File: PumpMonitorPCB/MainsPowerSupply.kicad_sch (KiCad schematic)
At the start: 26 parts, among them K1 J115F11CH5VDCS61-5U Relay, Q1 AS2302, U1 ACS770xCB-050B-PFF, U2 AMS1117-3.3

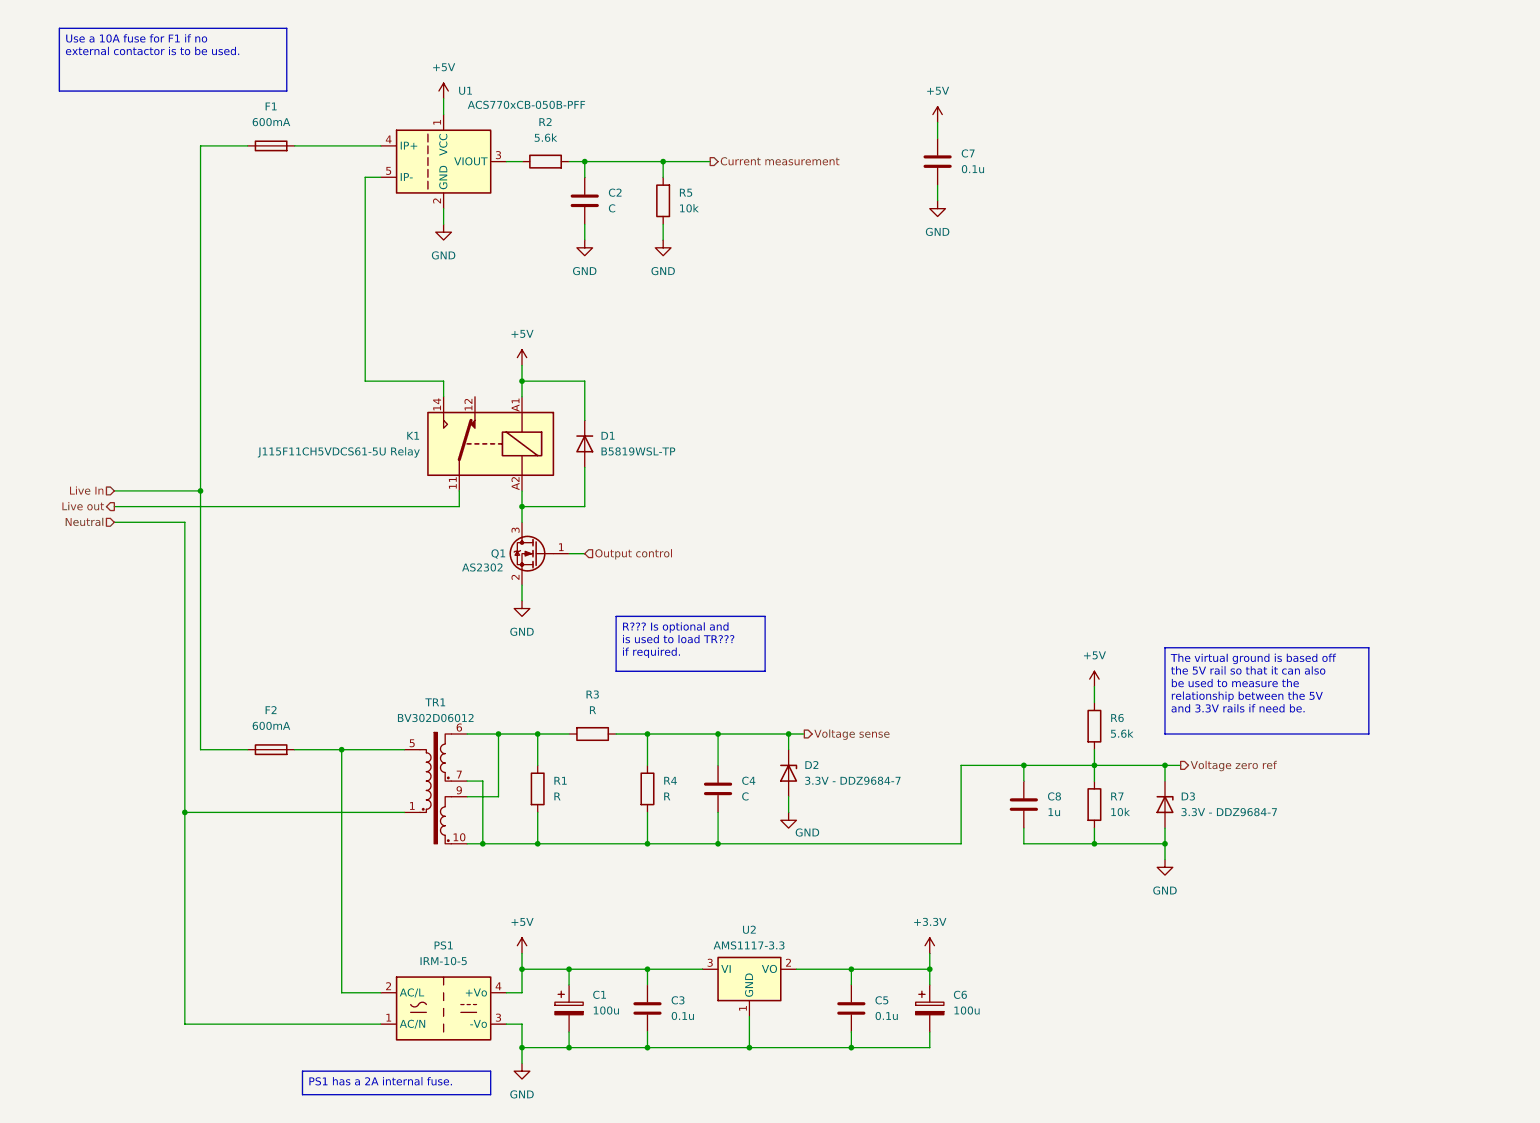
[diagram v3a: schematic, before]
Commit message: Added op amps to voltage and current measurement, more footprint assignments.
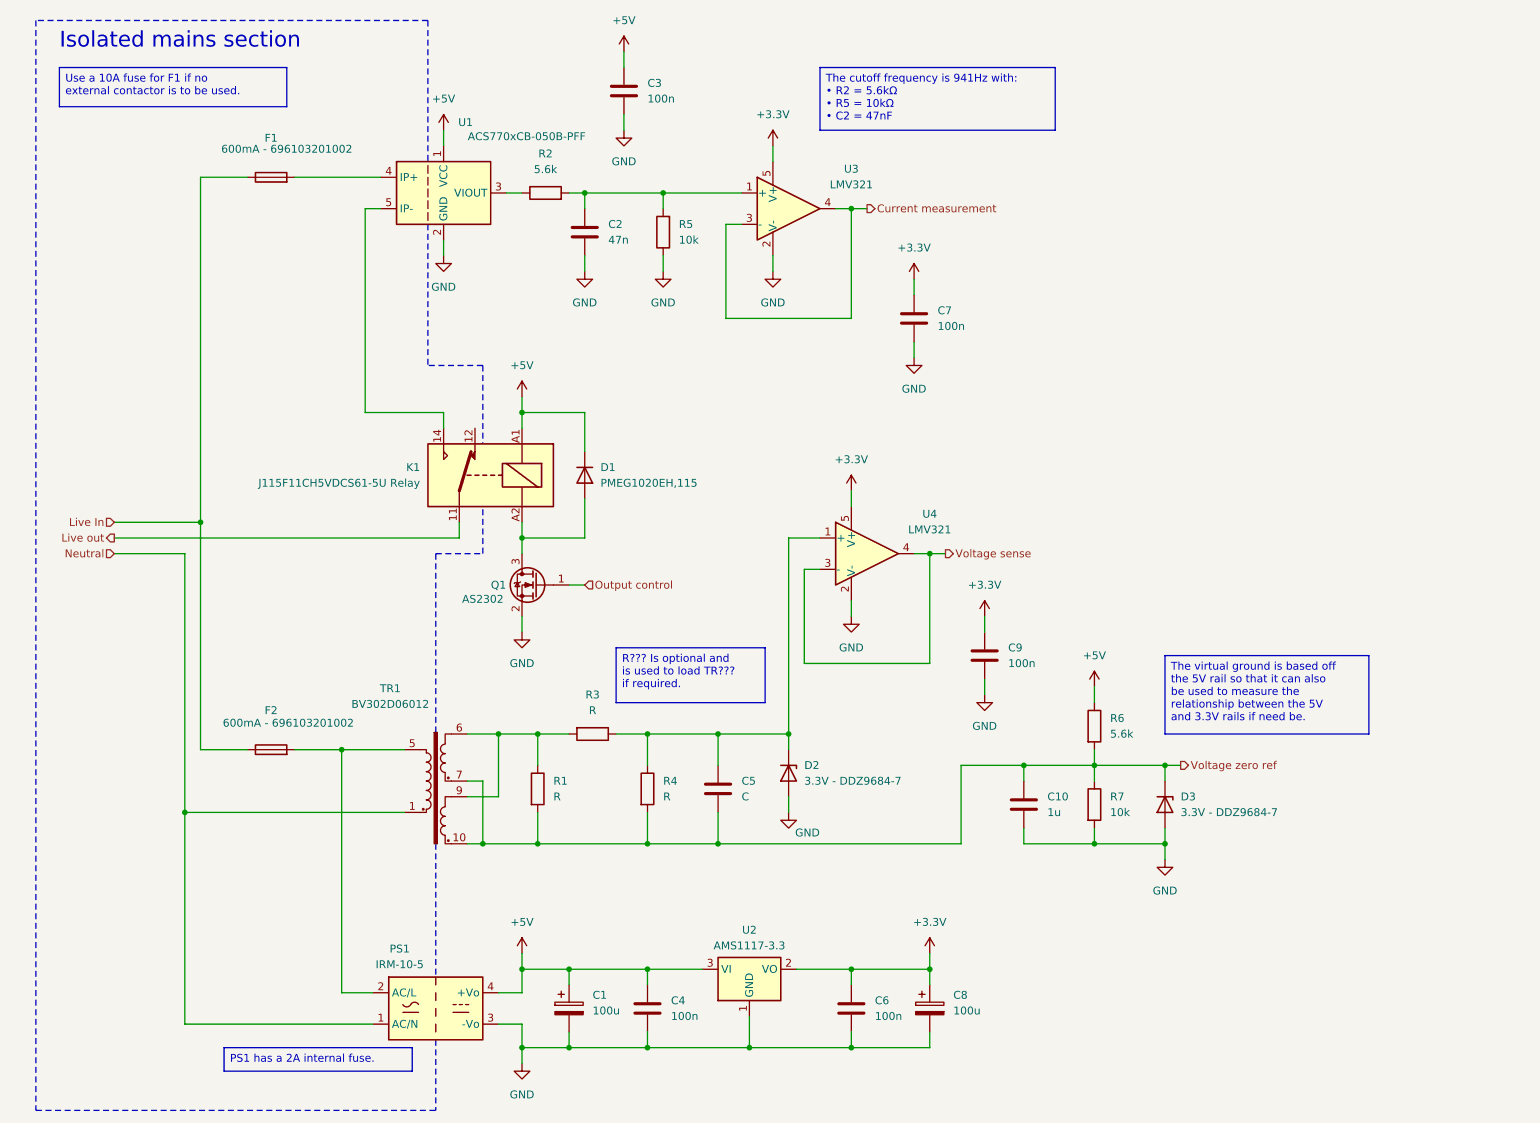
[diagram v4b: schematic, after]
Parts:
- added C7, C9: 100n, Capacitor_SMD:C_0805_2012Metric_Pad1.18x1.45mm_HandSolder, symbol Device:C
- added U3, U4: LMV321, Package_TO_SOT_SMD:SOT-23-5_HandSoldering, symbol Amplifier_Operational:LMV321
- C2: value C -> 47n
- C3: renamed from C7; value 0.1u -> 100n
- C4: renamed from C3; value 0.1u -> 100n
- C6: renamed from C5; value 0.1u -> 100n
- D1: value B5819WSL-TP -> PMEG1020EH,115; footprint Diode_SMD:D_SOD-323F -> Diode_SMD:D_SOD-123F
- F1, F2: value 600mA -> 600mA - 696103201002; footprint (none) -> Fuse:Fuseholder_Cylinder-5x20mm_Stelvio-Kontek_PTF78_Horizontal_Open
- renumbered C8 to C10, C4 to C5, C6 to C8
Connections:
- net +3.3V: now also C7.1, C9.1, U3.5 (V+), U4.5 (V+)
- net Current measurement: now also U3.3 (-), U3.4; no longer C2.1, R2.2, R5.2
- net GND: now also C7.2, C9.2, U3.2 (V-), U4.2 (V-)
- net Voltage sense: now also U4.3 (-), U4.4; no longer C5.1, D2.1 (K), R3.1, R4.1
- new net: C5.1, D2.1 (K), R3.1, R4.1, U4.1 (+)
- new net: C2.1, R2.2, R5.2, U3.1 (+)
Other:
- note added: "Isolated mains section"
- moved on the sheet: C2, C3, D1, F1, K1, PS1, Q1, R2, R5, U1

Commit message: Swapped current measurement to neutral (wiring diagram needs updating).
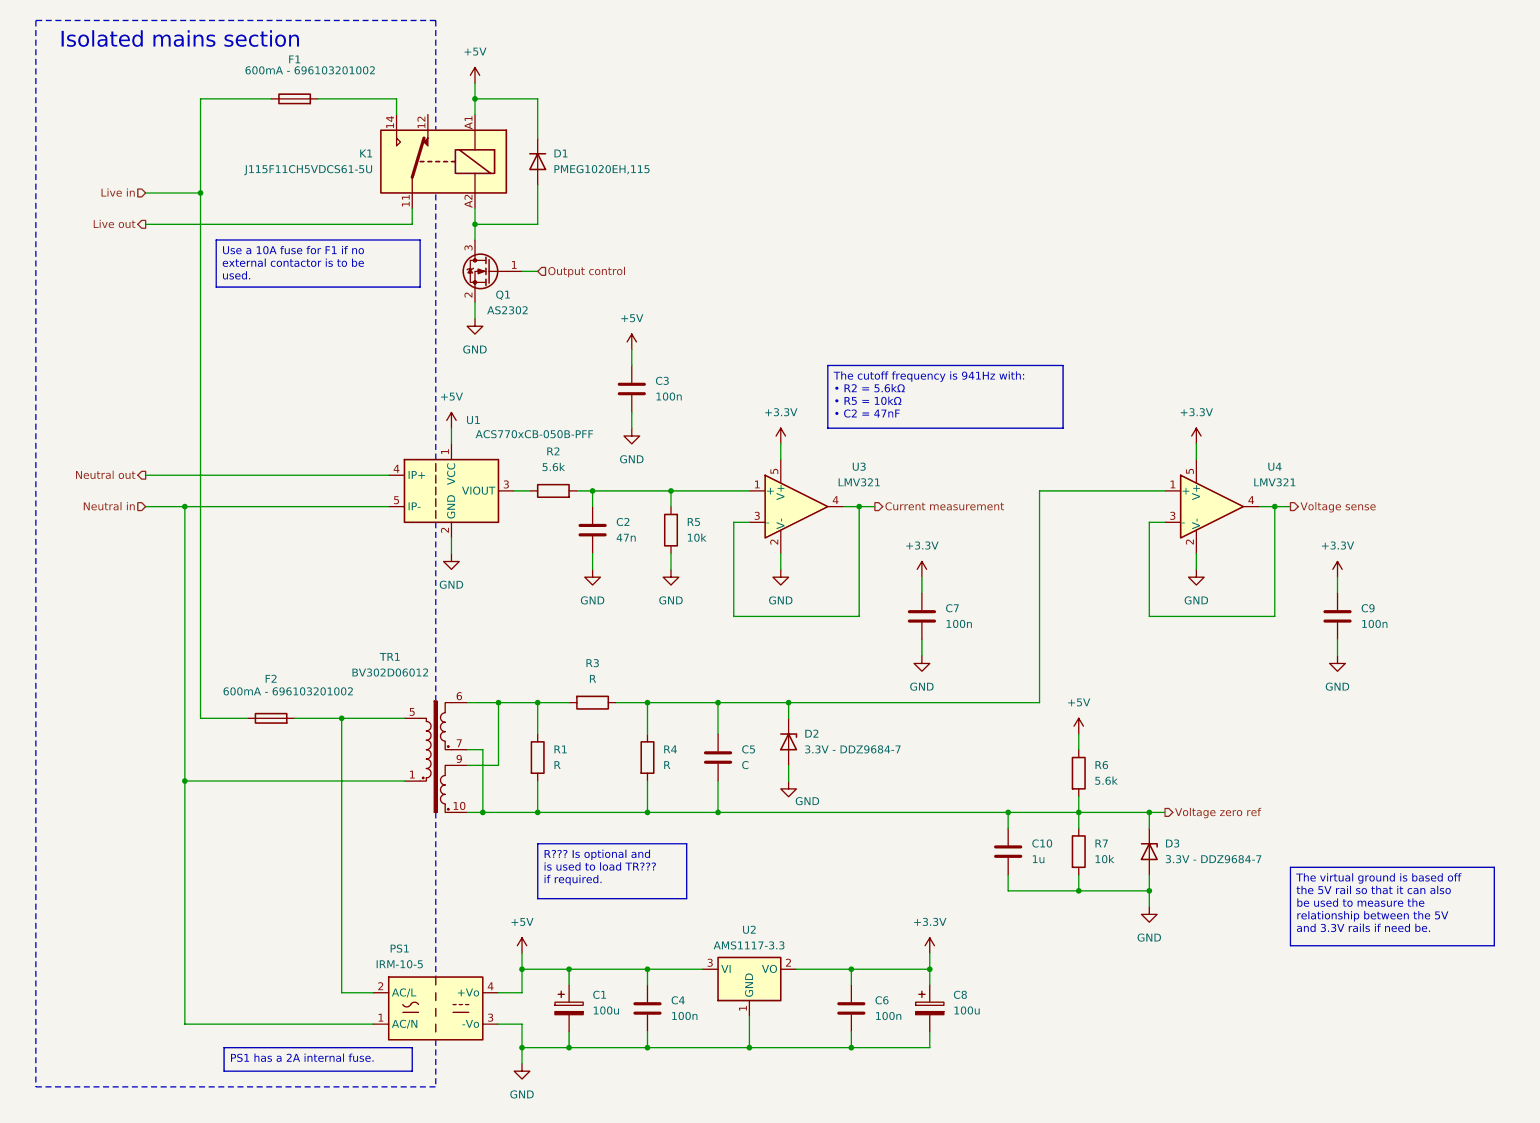
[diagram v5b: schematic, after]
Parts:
- K1: value J115F11CH5VDCS61-5U Relay -> J115F11CH5VDCS61-5U
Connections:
- net Neutral is gone; now on net Neutral in: PS1.1 (AC/N), TR1.1
- net at F1.2: now also K1.14; no longer U1.4 (IP+)
- net Neutral in: now reaches U1.5 (IP-)
- net Neutral in: no longer K1.14
- net Live In renamed Live in
- new net Neutral out: U1.4 (IP+)
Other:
- moved on the sheet: C10, C2, C3, C5, C7, C9, D1, D2, D3, F1, F2, K1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
